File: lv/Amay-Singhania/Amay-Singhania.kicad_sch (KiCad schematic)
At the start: 31 parts, among them IC1 TLV4888DR, J1 Conn_01x05

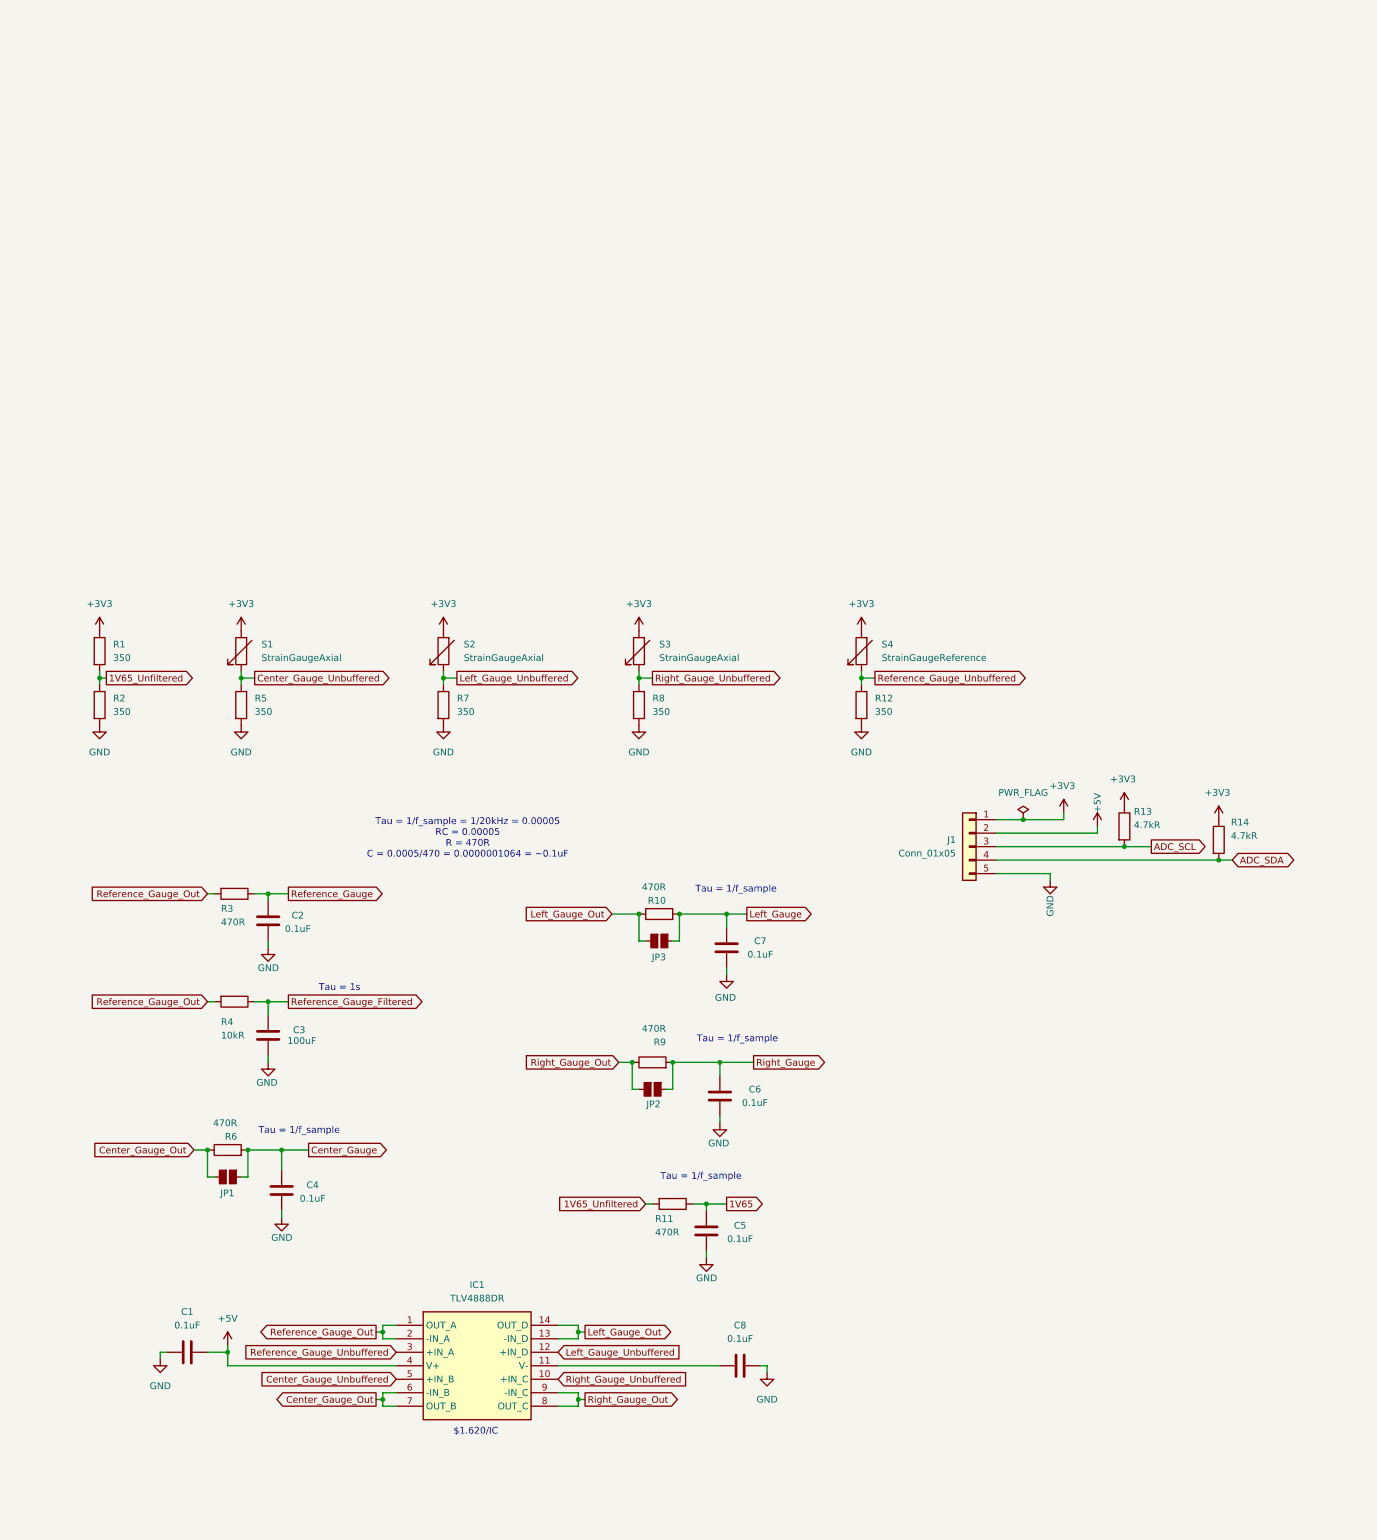
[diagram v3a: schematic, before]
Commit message: added voltage regulator and made schematic more readable by removing some global labels
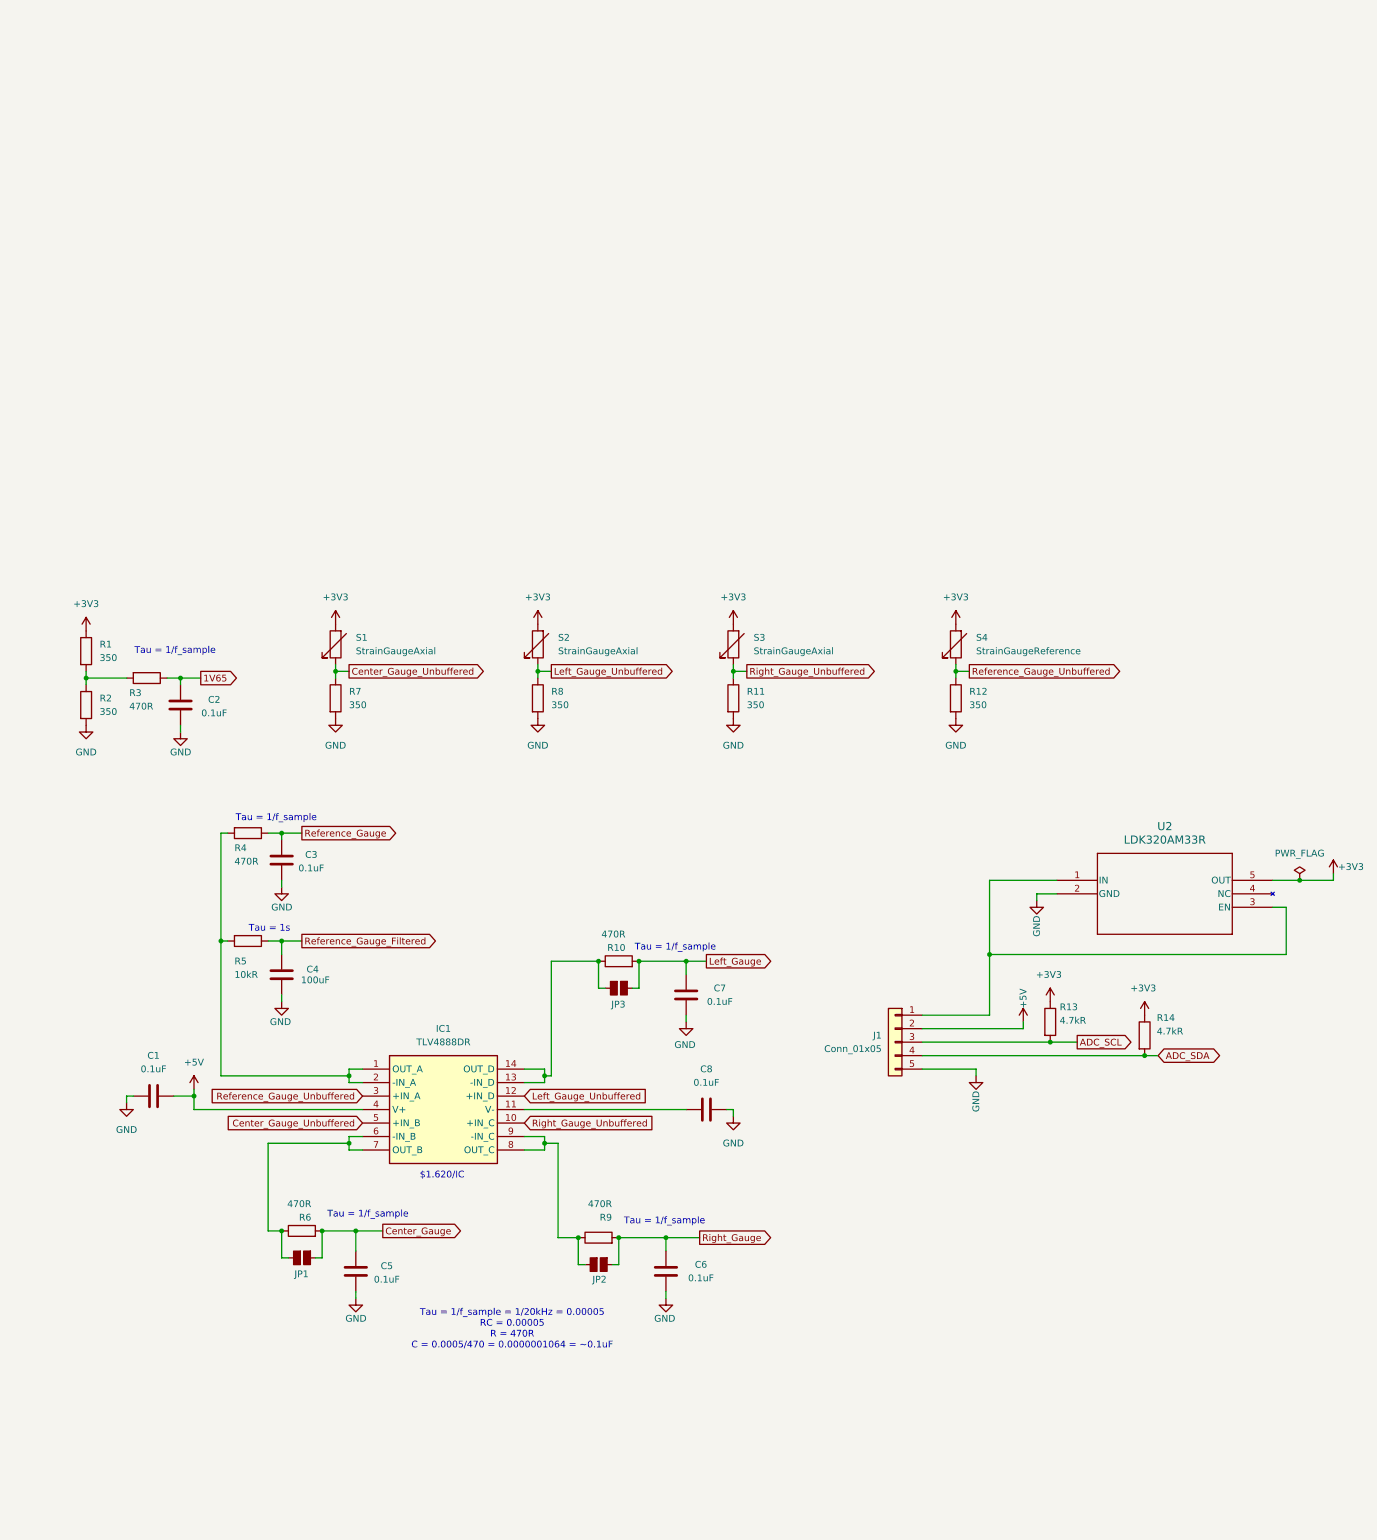
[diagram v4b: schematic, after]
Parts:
- added U2: LDK320AM33R, LDK320AM33R:SOT23-5L_STM, symbol LDK320AM33R:LDK320AM33R
- J1: footprint Package_DFN_QFN:QFN-20-1EP_5x5mm_P0.65mm_EP3.35x3.35mm -> (none)
- renumbered C5 to C2, C2 to C3, C3 to C4, C4 to C5, R8 to R11, R11 to R3, R3 to R4, R4 to R5, R5 to R7, R7 to R8
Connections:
- net +3V3: now also U2.5 (OUT); no longer J1.1 (Pin_1)
- net GND: now also U2.2 (GND)
- net 1V65_Unfiltered: no longer names the net of R1.2, R2.1, R3.2
- net Center_Gauge_Out: no longer names the net of IC1.6 (-IN_B), IC1.7 (OUT_B), JP1.2, R6.1
- net Left_Gauge_Out: no longer names the net of IC1.13 (-IN_D), IC1.14 (OUT_D), JP3.2, R10.1
- net Reference_Gauge_Out: no longer names the net of IC1.1 (OUT_A), IC1.2 (-IN_A), R4.2, R5.2
- net Right_Gauge_Out: no longer names the net of IC1.8 (OUT_C), IC1.9 (-IN_C), JP2.2, R9.1
- new net: J1.1 (Pin_1), U2.1 (IN), U2.3 (EN)
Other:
- moved on the sheet: C1, C2, C3, C4, C5, C6, C7, C8, IC1, J1, JP1, JP2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

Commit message: added voltage regulators and finished schematic
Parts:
- added U1: SL7550-3, Package_TO_SOT_SMD:SOT-23-3, symbol SL7550-3:SL75xx-3
- IC1: footprint TLV4888DR:SOIC127P600X175-14N -> SOIC127P600X175-14N
- J1: symbol Connector_Generic:Conn_01x05 -> Connector_Generic:Conn_01x04
- U2: footprint LDK320AM33R:SOT23-5L_STM -> SOT23-5L_STM
- renumbered C5 to C2, C2 to C3, C3 to C5, R8 to R10, R9 to R11, R10 to R12, R11 to R13, R12 to R14, R6 to R4, R13 to R6, R4 to R8, R14 to R9
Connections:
- net +5V: now also U2.1 (IN), U2.3 (EN), U1.2 (VOUT); no longer J1.2 (Pin_2)
- net ADC_SCL: now also J1.2 (Pin_2); no longer J1.3 (Pin_3)
- net ADC_SDA: now also J1.3 (Pin_3); no longer J1.4 (Pin_4)
- net GND: now also J1.4 (Pin_4), U1.1 (GND); no longer J1.5 (Pin_5)
- new net 12V_Input: J1.1 (Pin_1), U1.3 (VIN)
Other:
- note added: "+3V3 Regulator"
- note added: "+5V Regulator"
- note added: "TPB Input"
- note added: "Tau = 1/f_sample = 1/20kHz = 0.00005 RC = 0.00005 R = 470R C = 0.0005/470 = 0.0000001064 = ~0.1uF Total current draw of op amp and RCs: 5v/(sqrt(470R^2 + (1/(2 * pi * 20kHz * 0.1uF))^2)) = 10.49mA * 4 = 41.96 mA 5v/(sqrt(10kR^2 + (1/(2 * pi * 1Hz * 100uF))^2)) = 0.5 mA 41.96 mA + 0.5 mA = 42.46 mA"
- note removed: "Tau = 1/f_sample = 1/20kHz = 0.00005 RC = 0.00005 R = 470R C = 0.0005/470 = 0.0000001064 = ~0.1uF"
- moved on the sheet: C1, C2, C4, C5, C6, C7, C8, IC1, JP1, JP2, JP3, R11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

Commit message: final commit to onboarding, moved to fpc-strain-gauge in fs-5-schematics repo
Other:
- note added: "TSV914IDT - $1.15 MCP3564RT-E/ST - $5.44 LDK320AM33R - $0.65 --------------------- Total - 7.24"
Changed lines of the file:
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@@
+		)
+	)
+	(text "TSV914IDT - $1.15\nMCP3564RT-E/ST - $5.44\nLDK320AM33R - $0.65\n---------------------\nTotal - 7.24"
+		(exclude_from_sim no)
+		(at 208.788 99.314 0)
+		(effects
+			(font
+				(size 1.27 1.27)
+			)
 		)
 	)
